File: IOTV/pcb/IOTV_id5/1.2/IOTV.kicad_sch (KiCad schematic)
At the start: 23 parts, among them J1 Screw_Terminal_01x02, J2 Screw_Terminal_01x02, J3 Conn_01x04, J4 Conn_01x04, J5 Conn_01x04, J6 Conn_01x05, J8 UART, SW1 RST, SW2 Boot, U1 ESP32-WROOM-E, U2 G7DA-28 (Z)D3 8A/240V (3-32V)

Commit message: pcb id5 rev 1.2
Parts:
- U2: footprint OptoDevice:Finder_34.81 -> Library:G7DA-28
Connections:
- net U0RX: now also J8.3 (Pin_3); no longer J8.2 (Pin_2)
- net U0TX: now also J8.2 (Pin_2); no longer J8.3 (Pin_3)
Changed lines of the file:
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@@
     )
   )
-  (global_label "U0TX" (shape bidirectional) (at 43.18 144.145 180) (fields_autoplaced)
-    (effects (font (size 1.27 1.27)) (justify right))
-    (property "Intersheetrefs" "${INTERSHEET_REFS}" (at 34.4458 144.145 0)
+  (global_label "U0TX" (shape bidirectional) (at 43.18 141.605 180) (fields_autoplaced)
+    (effects (font (size 1.27 1.27)) (justify right))
+    (property "Intersheetrefs" "${INTERSHEET_REFS}" (at 34.4458 141.605 0)
       (effects (font (size 1.27 1.27)) (justify right))
     )
@@
     )
   )
-  (global_label "U0RX" (shape bidirectional) (at 43.18 141.605 180) (fields_autoplaced)
-    (effects (font (size 1.27 1.27)) (justify right))
-    (property "Intersheetrefs" "${INTERSHEET_REFS}" (at 34.1434 141.605 0)
+  (global_label "U0RX" (shape bidirectional) (at 43.18 144.145 180) (fields_autoplaced)
+    (effects (font (size 1.27 1.27)) (justify right))
+    (property "Intersheetrefs" "${INTERSHEET_REFS}" (at 34.1434 144.145 0)
       (effects (font (size 1.27 1.27)) (justify right))
     )
@@
       (effects (font (size 1.27 1.27)) (justify right))
     )
-    (property "Footprint" "OptoDevice:Finder_34.81" (at 185.42 44.45 0)
-      (effects (font (size 1.27 1.27) italic) (justify left) hide)
+    (property "Footprint" "Library:G7DA-28" (at 185.42 44.45 0)
+      (effects (font (size 1.27 1.27) italic) (justify left))
     )
     (property "Datasheet" "http://www.us.liteon.com/downloads/LTV-817-827-847.PDF" (at 190.5 39.37 0)

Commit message: MK id5 1.1
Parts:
- added Q1: S8050, Package_TO_SOT_SMD:SOT-23, symbol Simulation_SPICE:NPN
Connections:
- net +3.3V: now also Q1.3 (C)
- net GPIO32: now reaches U1.8 (32K_XP/GPIO32/ADC1_CH4)
- net GPIO32: now also Q1.1 (B)
- net GPIO34: no longer names the net of U1.6 (GPIO34/ADC1_CH6)
- net GPIO34: no longer U2.A1
- new net ssr+: Q1.2 (E), U2.A1
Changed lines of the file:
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@@
   (no_connect (at 76.2 108.585))
   (no_connect (at 142.24 116.205))
+  (no_connect (at 76.2 103.505))
   (no_connect (at 142.24 111.125))
   (no_connect (at 142.24 103.505))
@@
   (no_connect (at 76.2 98.425))
   (no_connect (at 142.24 90.805))
-  (no_connect (at 76.2 83.185))
   (no_connect (at 76.2 85.725))
   (no_connect (at 192.405 85.725))
@@
     (stroke (width 0) (type default))
   )
+  (wire (pts (xy 73.66 103.505) (xy 73.66 83.185))
+    (stroke (width 0) (type default))
+  )
   (wire (pts (xy 93.98 152.4) (xy 96.52 152.4))
     (stroke (width 0) (type default))
@@
     (stroke (width 0) (type default))
   )
-  (wire (pts (xy 71.12 103.505) (xy 76.2 103.505))
-    (stroke (width 0) (type default))
-  )
   (wire (pts (xy 83.82 152.4) (xy 88.9 152.4))
     (stroke (width 0) (type default))
   )
+  (wire (pts (xy 73.66 83.185) (xy 76.2 83.185))
+    (stroke (width 0) (type default))
+  )
   (wire (pts (xy 96.52 146.05) (xy 96.52 152.4))
     (stroke (width 0) (type default))
@@
     (stroke (width 0) (type default))
   )
+  (wire (pts (xy 71.12 103.505) (xy 73.66 103.505))
+    (stroke (width 0) (type default))
+  )
   (wire (pts (xy 35.56 62.865) (xy 35.56 66.675))
     (stroke (width 0) (type default))
@@
     )
   )
+  (global_label "ssr+" (shape bidirectional) (at 171.45 62.23 0) (fields_autoplaced)
+    (effects (font (size 1.27 1.27)) (justify left))
+    (property "Intersheetrefs" "${INTERSHEET_REFS}" (at 179.8819 62.23 0)
+      (effects (font (size 1.27 1.27)) (justify left))
+    )
+  )
   (global_label "U0TX" (shape bidirectional) (at 43.18 141.605 180) (fields_autoplaced)
     (effects (font (size 1.27 1.27)) (justify right))
@@
     )
   )
-  (global_label "GPIO34" (shape bidirectional) (at 71.12 103.505 180) (fields_autoplaced)
+  (global_label "GPIO32" (shape bidirectional) (at 71.12 103.505 180) (fields_autoplaced)
     (effects (font (size 1.27 1.27)) (justify right))
     (property "Intersheetrefs" "${INTERSHEET_REFS}" (at 60.2086 103.505 0)
@@
     )
   )
+  (global_label "GPIO32" (shape bidirectional) (at 166.37 68.58 270) (fields_autoplaced)
+    (effects (font (size 1.27 1.27)) (justify right))
+    (property "Intersheetrefs" "${INTERSHEET_REFS}" (at 166.37 79.4914 90)
+      (effects (font (size 1.27 1.27)) (justify right))
+    )
+  )
   (global_label "SDA" (shape bidirectional) (at 192.405 107.95 180) (fields_autoplaced)
     (effects (font (size 1.27 1.27)) (justify right))
@@
     )
   )
-  (global_label "GPIO34" (shape bidirectional) (at 193.04 46.99 270) (fields_autoplaced)
-    (effects (font (size 1.27 1.27)) (justify right))
-    (property "Intersheetrefs" "${INTERSHEET_REFS}" (at 193.04 57.9014 90)
-      (effects (font (size 1.27 1.27)) (justify right))
-    )
-  )
   (global_label "SDA" (shape bidirectional) (at 142.24 106.045 0) (fields_autoplaced)
     (effects (font (size 1.27 1.27)) (justify left))
@@
     )
   )
+  (global_label "ssr+" (shape bidirectional) (at 193.04 46.99 270) (fields_autoplaced)
+    (effects (font (size 1.27 1.27)) (justify right))
+    (property "Intersheetrefs" "${INTERSHEET_REFS}" (at 193.04 55.4219 90)
+      (effects (font (size 1.27 1.27)) (justify right))
+    )
+  )
   (global_label "+3.3V" (shape bidirectional) (at 43.18 146.685 180) (fields_autoplaced)
     (effects (font (size 1.27 1.27)) (justify right))
@@
     (effects (font (size 1.27 1.27)) (justify right))
     (property "Intersheetrefs" "${INTERSHEET_REFS}" (at 184.8198 96.52 0)
+      (effects (font (size 1.27 1.27)) (justify right))
+    )
+  )
+  (global_label "+3.3V" (shape bidirectional) (at 161.29 62.23 180) (fields_autoplaced)
+    (effects (font (size 1.27 1.27)) (justify right))
+    (property "Intersheetrefs" "${INTERSHEET_REFS}" (at 151.5881 62.23 0)
       (effects (font (size 1.27 1.27)) (justify right))
     )
@@
         )
       )
+    )
+  )
+  (symbol (lib_id "Simulation_SPICE:NPN") (at 166.37 64.77 90) (unit 1)
+    (in_bom yes) (on_board yes) (dnp no) (fields_autoplaced)
+    (property "Reference" "Q1" (at 166.37 57.15 90)
+      (effects (font (size 1.27 1.27)))
+    )
+    (property "Value" "S8050" (at 166.37 59.69 90)
+      (effects (font (size 1.27 1.27)))
+    )
+    (property "Footprint" "Package_TO_SOT_SMD:SOT-23" (at 166.37 1.27 0)
+      (effects (font (size 1.27 1.27)) hide)
+    )
+    (property "Datasheet" "~" (at 166.37 1.27 0)
+      (effects (font (size 1.27 1.27)) hide)
+    )
+    (property "Sim.Device" "NPN" (at 166.37 64.77 0)
+      (effects (font (size 1.27 1.27)) hide)
+    )
+    (property "Sim.Type" "GUMMELPOON" (at 161.29 63.5 0)
+      (effects (font (size 1.27 1.27)) hide)
+    )
+    (property "Sim.Pins" "1=B 2=E 3=C" (at 171.45 64.77 0)
+      (effects (font (size 1.27 1.27)) hide)
+    )
+    (pin "1")
+    (pin "2")
+    (pin "3")
+    (instances
+      (project "IOTV"
+        (path "/1ca02c68-d763-4d2d-aed4-975a014c3931"
+          (reference "Q1") (unit 1)
+        )
+      )

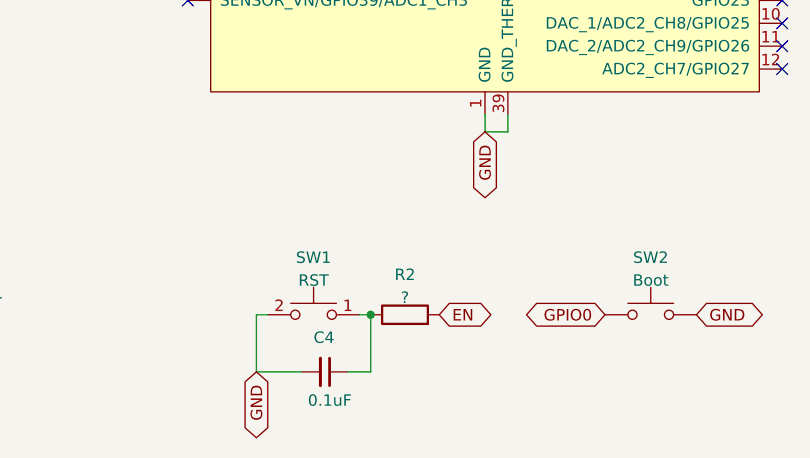
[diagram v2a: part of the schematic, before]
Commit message: потоки чтения и записи
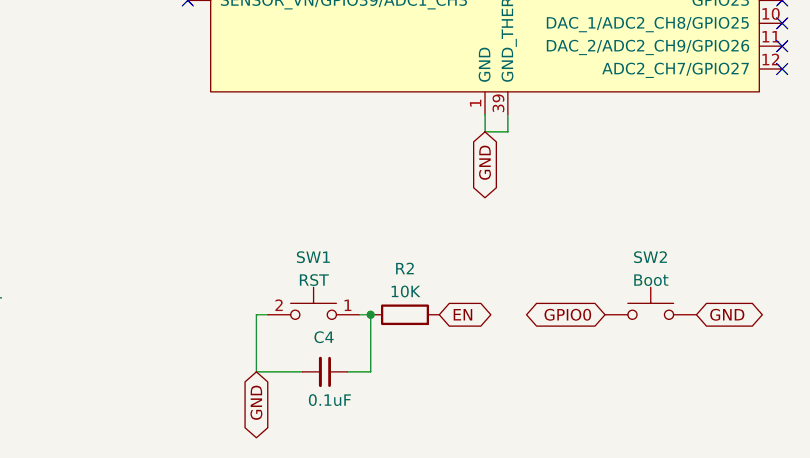
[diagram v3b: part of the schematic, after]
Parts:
- R2: value ? -> 10K
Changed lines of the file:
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@@
   (symbol (lib_id "Device:R") (at 100.33 146.05 90) (unit 1)
     (in_bom yes) (on_board yes) (dnp no) (fields_autoplaced)
-    (property "Reference" "R2" (at 100.33 141.605 90)
+    (property "Reference" "R2" (at 100.33 140.97 90)
       (effects (font (size 1.27 1.27)))
     )
-    (property "Value" "?" (at 100.33 144.145 90)
+    (property "Value" "10K" (at 100.33 143.51 90)
       (effects (font (size 1.27 1.27)))
     )

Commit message: pcb id5
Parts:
- R2: value 10K -> 5K
